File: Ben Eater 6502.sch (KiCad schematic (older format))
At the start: 3 parts, among them SW1 Reset, U1 W65C02SxP

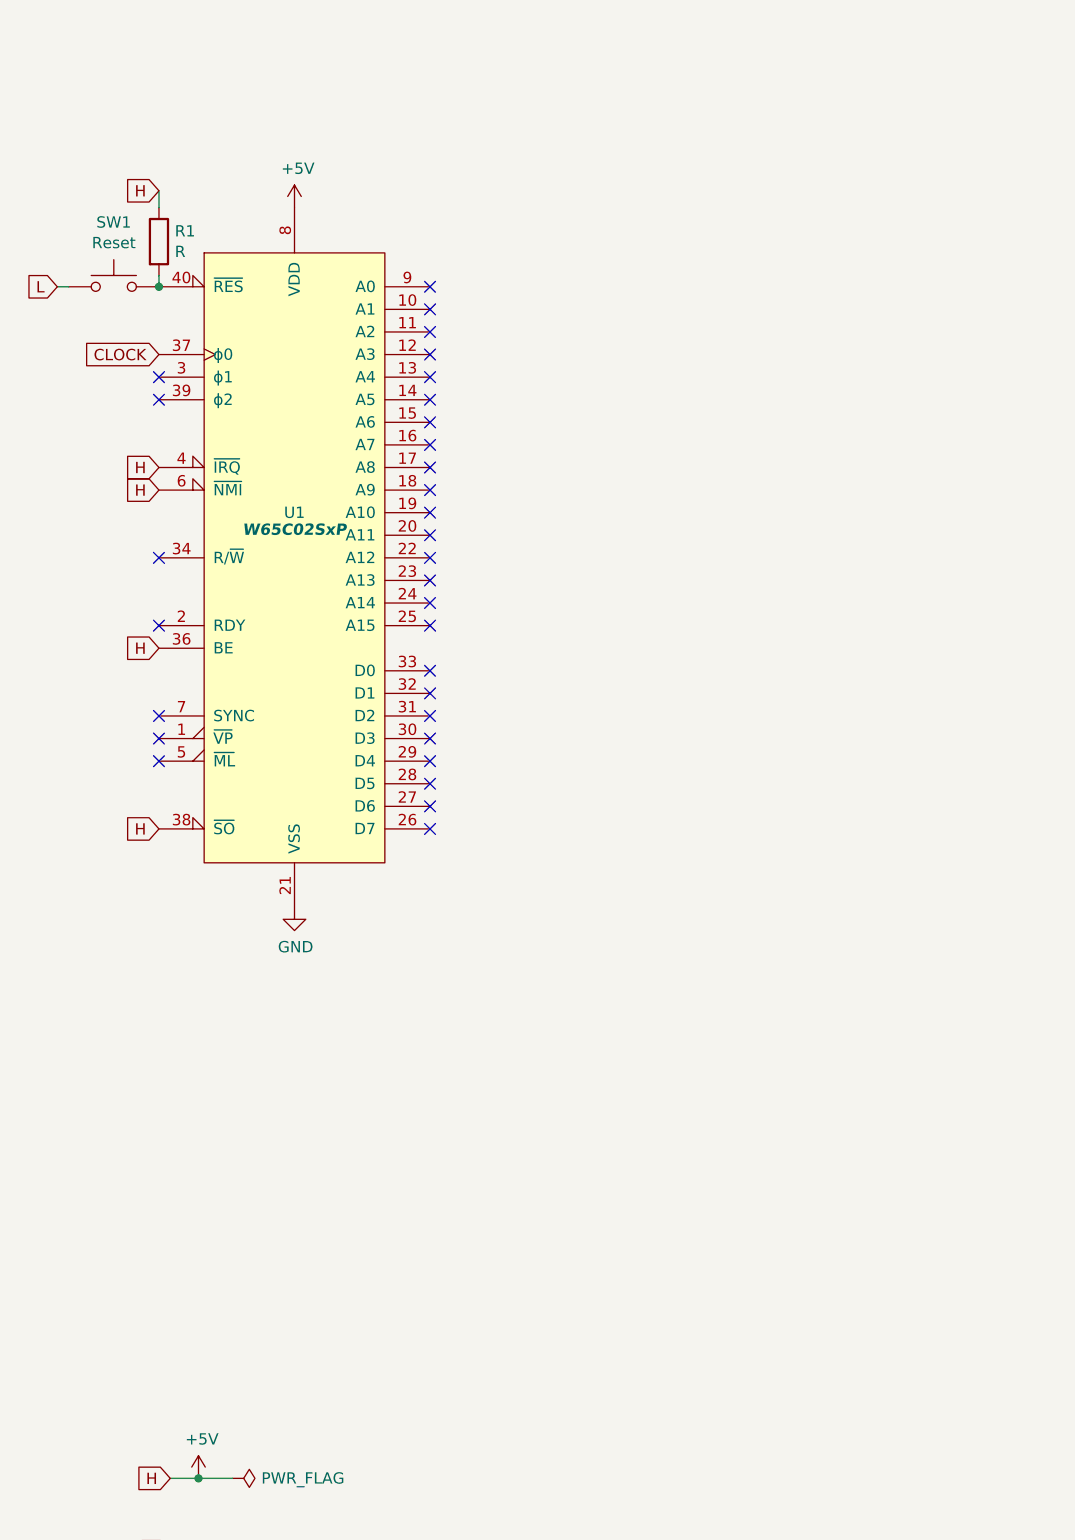
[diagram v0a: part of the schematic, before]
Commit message: Stage 2a
Added rom
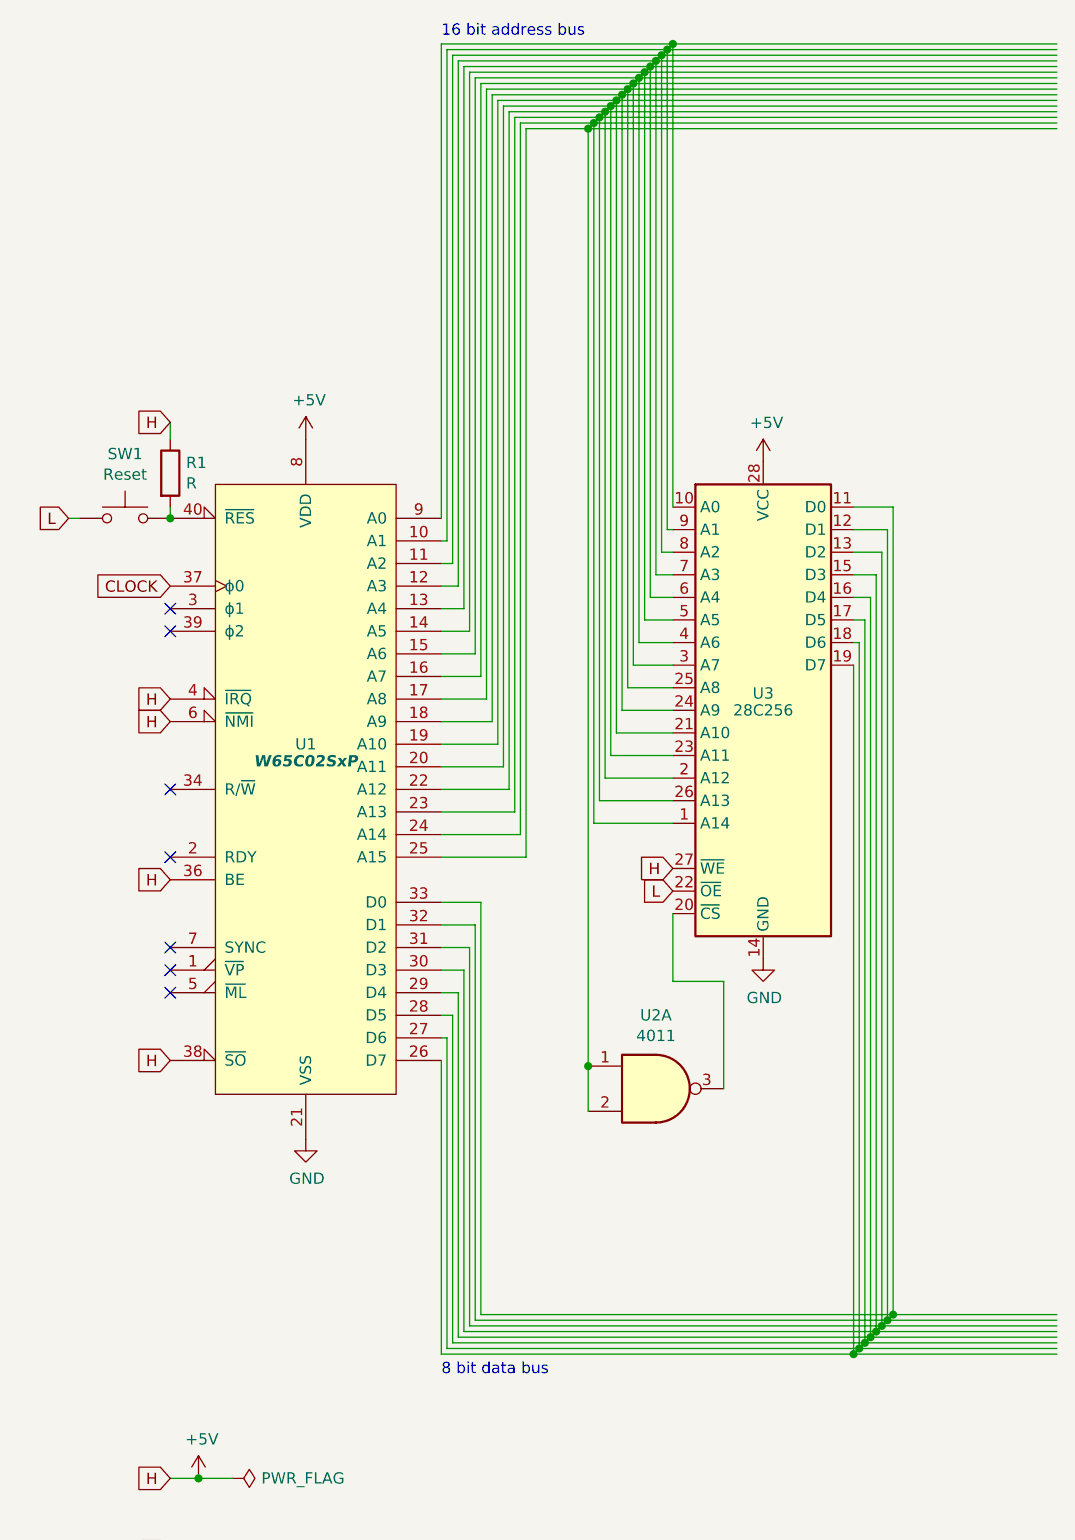
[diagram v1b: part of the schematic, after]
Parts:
- added U2: 4011, symbol 4xxx:4011
- added U3: 28C256, symbol Memory_EEPROM:28C256
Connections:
- wire segments 7 -> 150
- no-connect marks 31 -> 7
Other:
- note added: "16 bit address bus"
- note added: "8 bit data bus"
- moved on the sheet: R1, SW1, U1

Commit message: Stage 2b
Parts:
- added U4: 4011, symbol 4xxx:4011
- added U5: W65C22SxP, symbol 65xx:W65C22SxP
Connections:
- wire segments 150 -> 221
- no-connect marks 7 -> 27

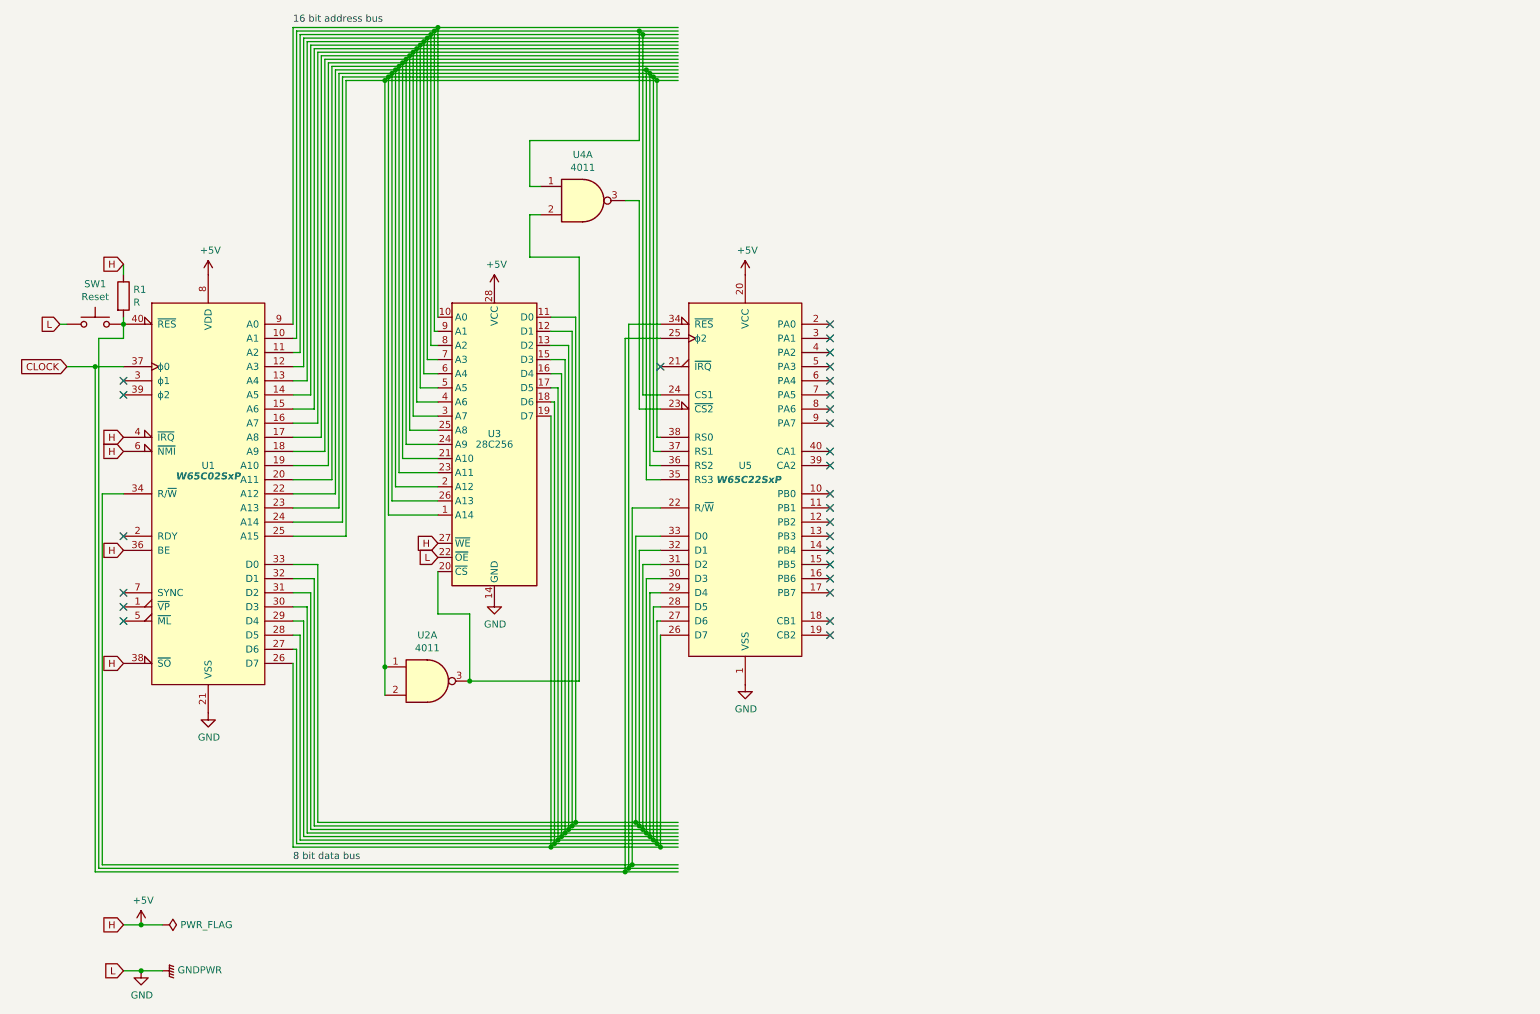
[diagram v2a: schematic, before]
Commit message: Redo phase 2 with bus lines
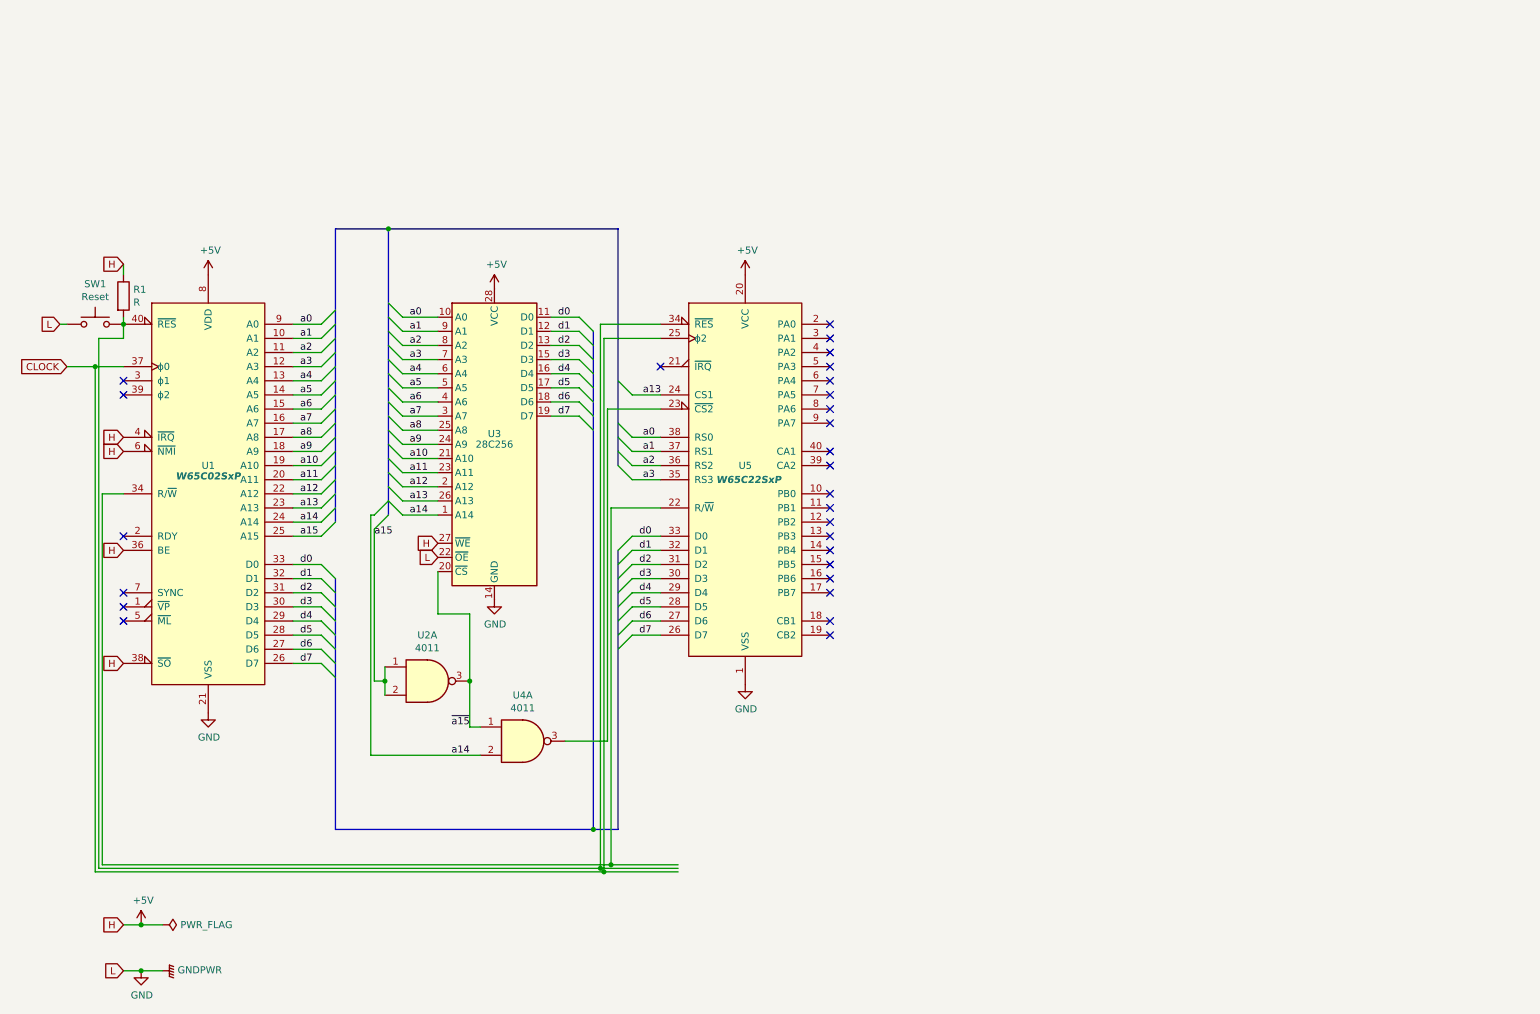
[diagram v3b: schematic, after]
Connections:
- net labels added: a0, a1, a10, a11, a12, a13, a14, a15, a2, a3, a4, a5, a6, a7, a8, a9, d0, d1, d2, d3, d4, d5, d6, d7, ~a15
- wire segments 221 -> 102
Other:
- note removed: "16 bit address bus"
- note removed: "8 bit data bus"
- moved on the sheet: U4A

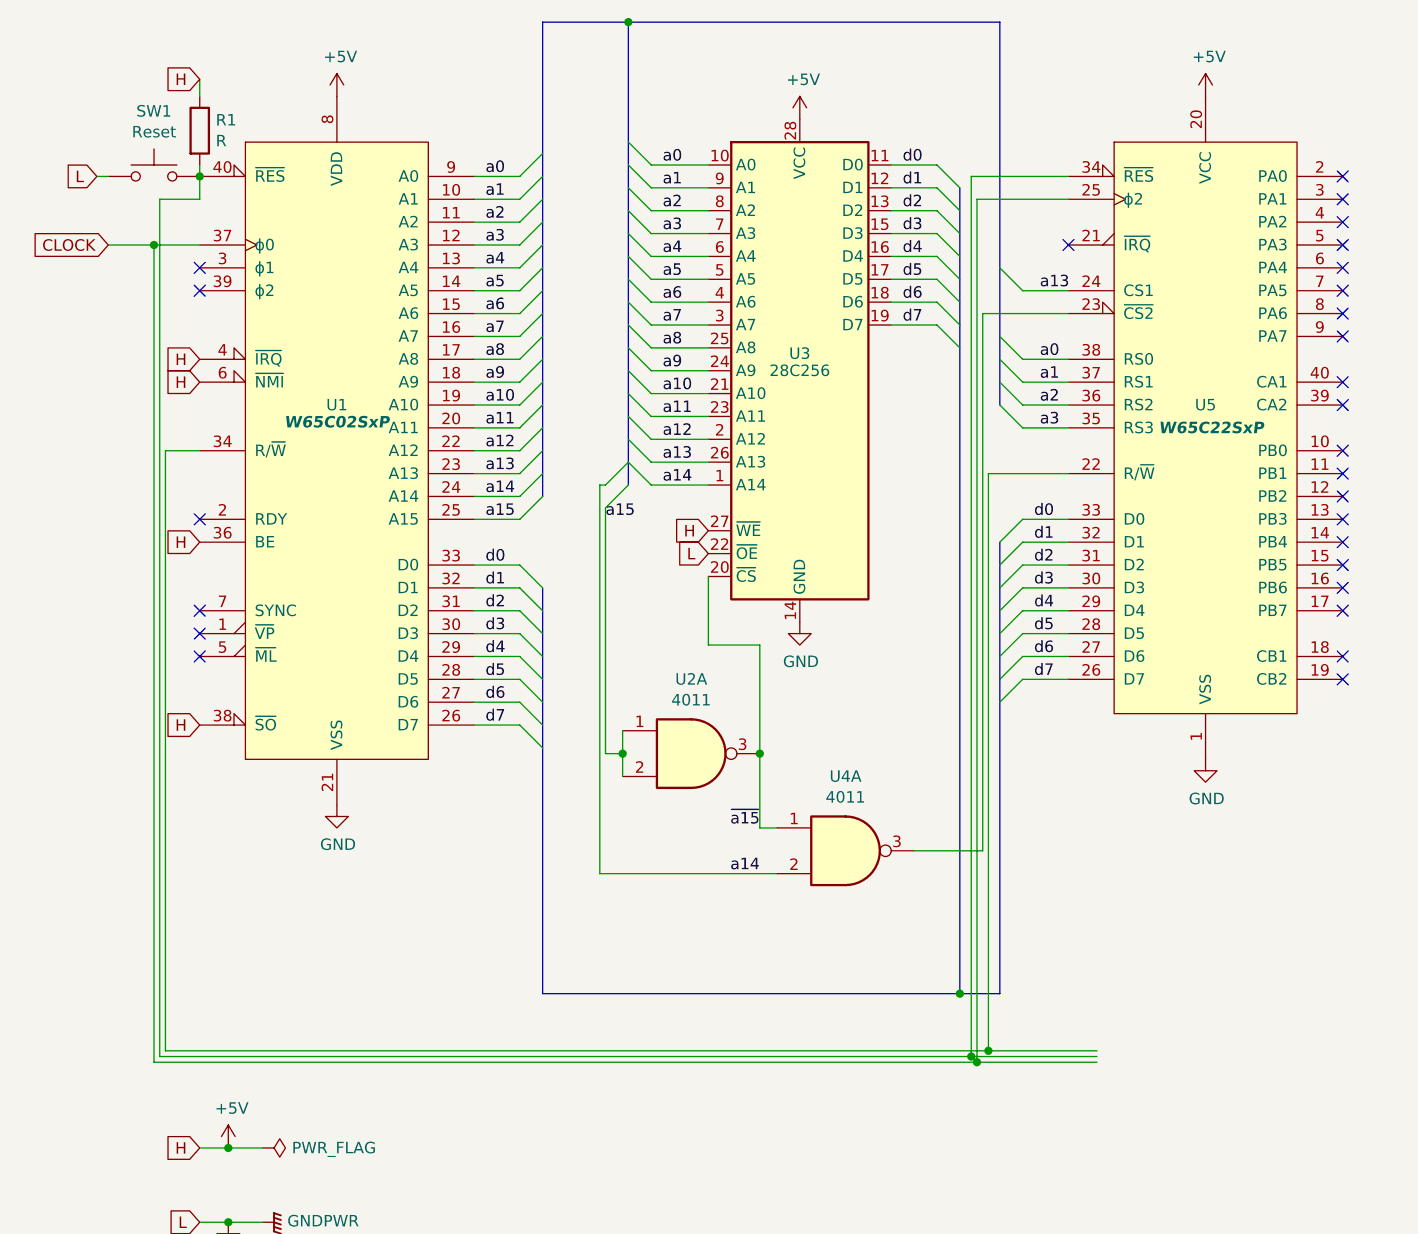
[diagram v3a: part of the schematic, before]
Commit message: Connect 6502/RDY. Space wires out a bit better
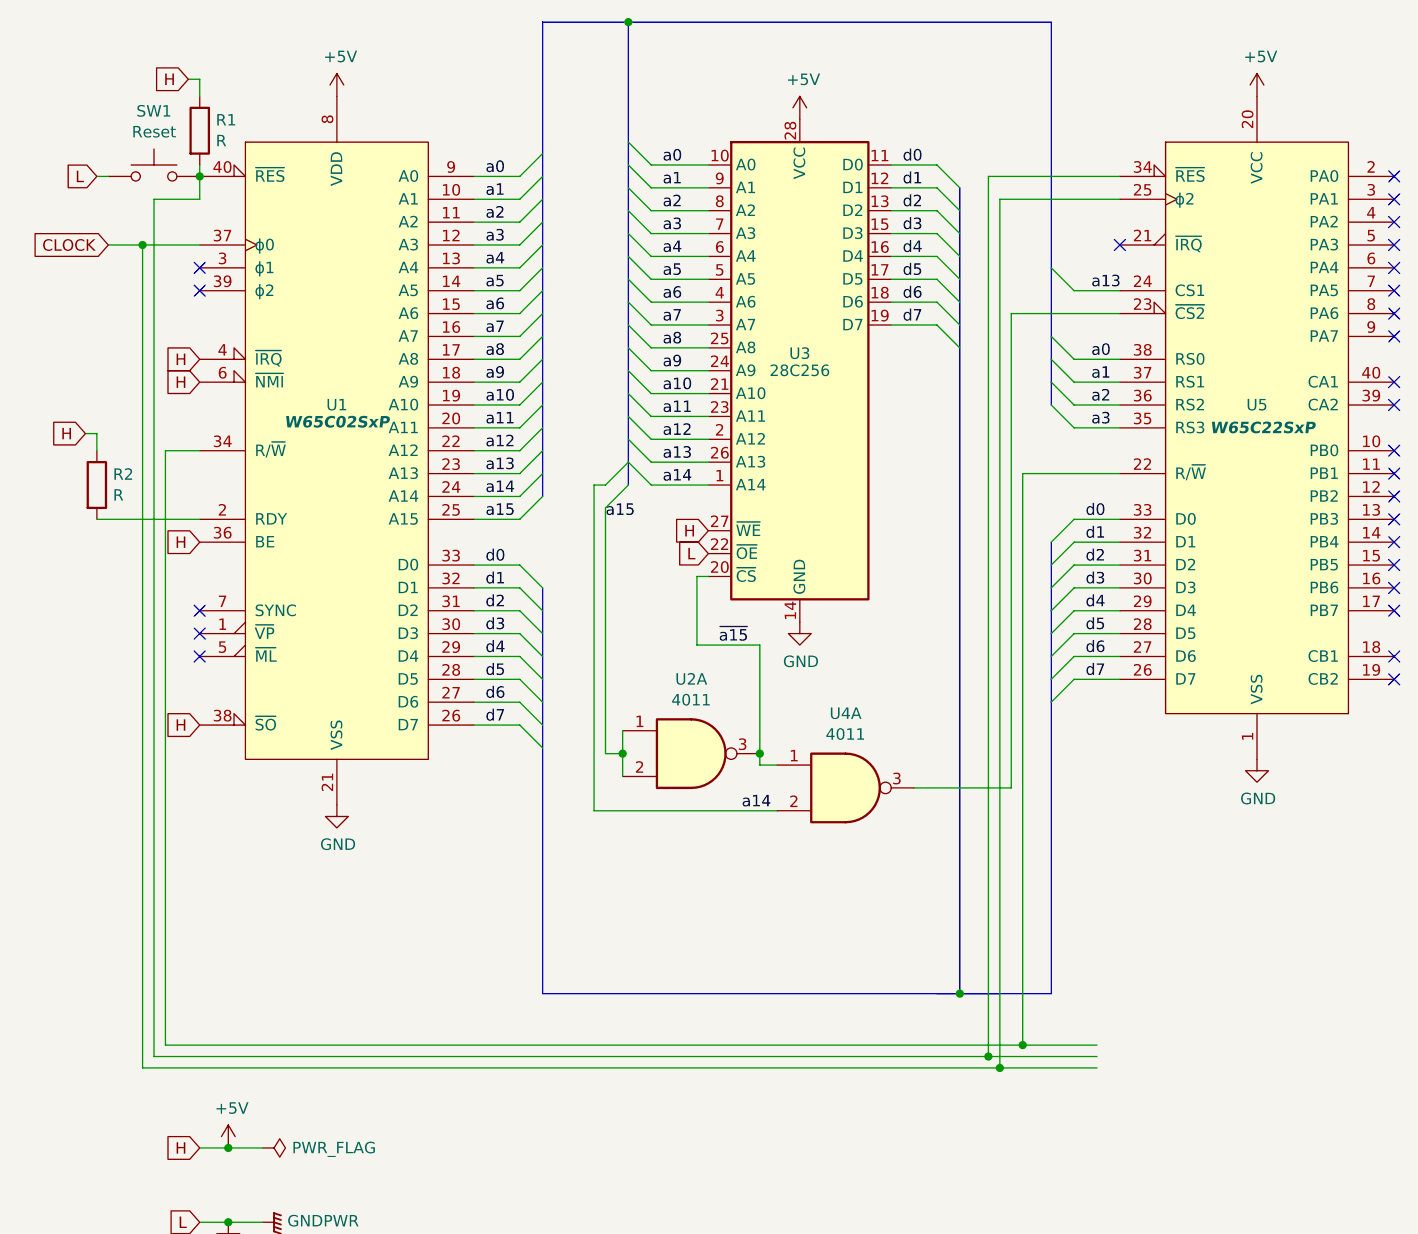
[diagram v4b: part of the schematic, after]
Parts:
- added R2: R, symbol Device:R
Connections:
- net +5V: now also R2.1
- net at U1.2 (RDY): now also R2.2
- no-connect marks 27 -> 26
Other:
- moved on the sheet: U4A, U5
